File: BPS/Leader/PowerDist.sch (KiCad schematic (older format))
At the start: 15 parts, among them J5 PowerConn, U2 RI3-1205S, U3 NCP1117-3.3_SOT223

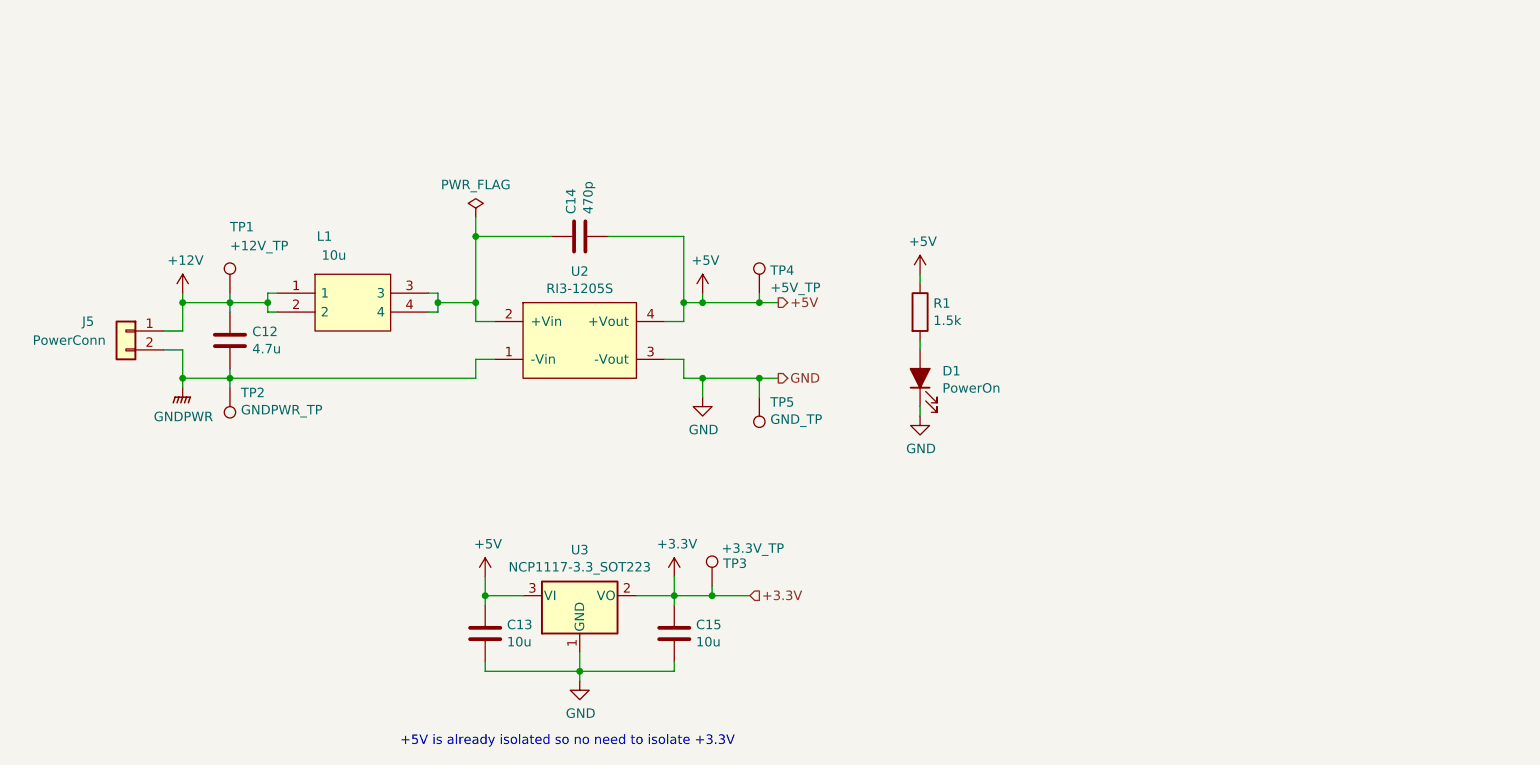
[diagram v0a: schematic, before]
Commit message: Places most components of leader board in their respective locations with nothing traced
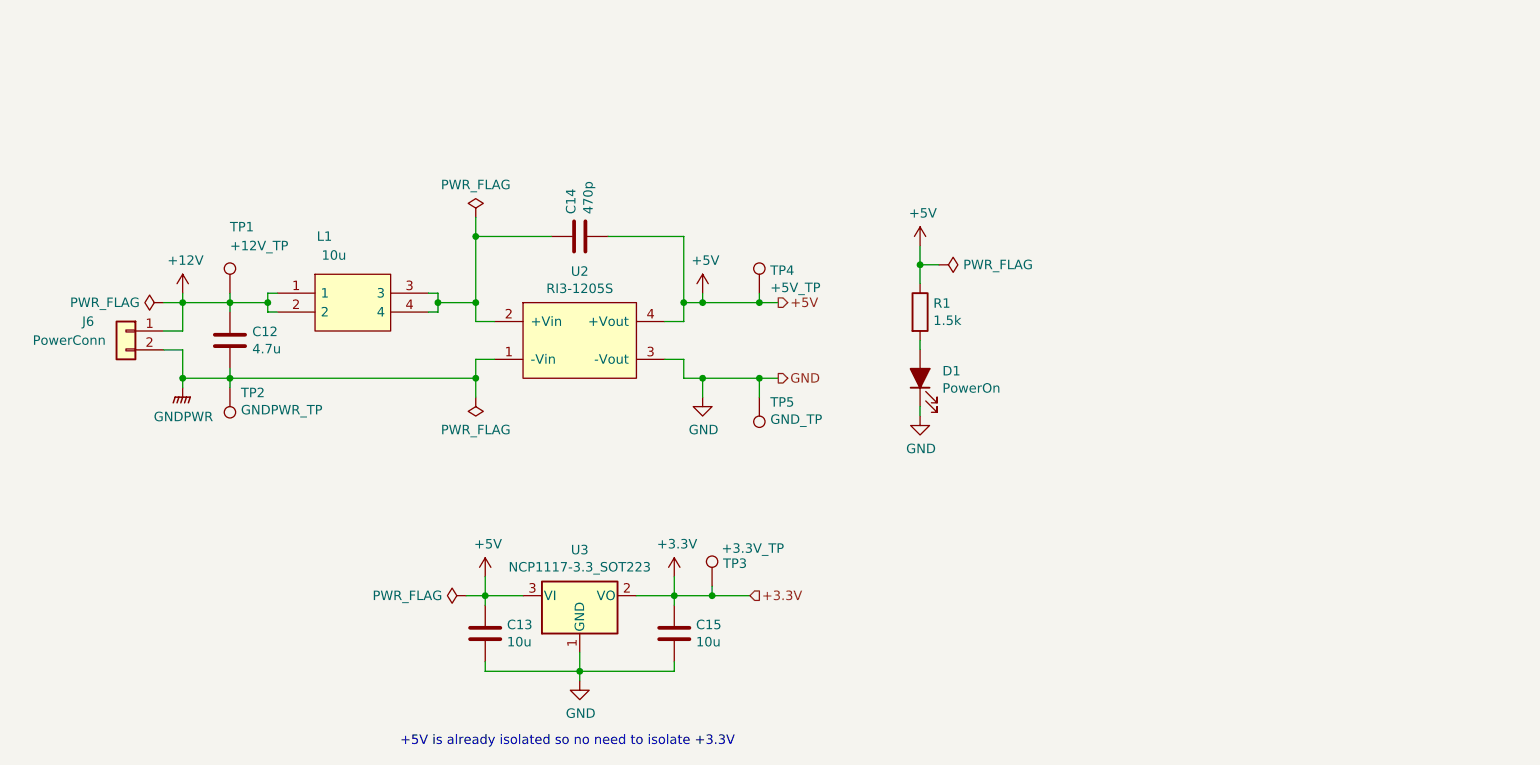
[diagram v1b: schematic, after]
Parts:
- J6: renamed from J5; footprint Connector_Molex:Molex_Micro-Fit_3.0_43650-0215_1x02_P3.00mm_Vertical -> UTSVT_Connectors:Molex_MicroFit3.0_1x2xP3.00mm_PolarizingPeg_Vertical
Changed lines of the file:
@@
 L power:+5V #PWR028
 U 1 1 5C58FEF6
-P 6350 3050
-F 0 "#PWR028" H 6350 2900 50  0001 C CNN
-F 1 "+5V" H 6365 3223 50  0000 C CNN
-F 2 "" H 6350 3050 50  0001 C CNN
-F 3 "" H 6350 3050 50  0001 C CNN
-	1    6350 3050
-	1    0    0    -1
-$EndComp
-Wire Wire Line
-	6350 3050 6350 3100
+P 6350 2900
+F 0 "#PWR028" H 6350 2750 50  0001 C CNN
+F 1 "+5V" H 6365 3073 50  0000 C CNN
+F 2 "" H 6350 2900 50  0001 C CNN
+F 3 "" H 6350 2900 50  0001 C CNN
+	1    6350 2900
+	1    0    0    -1
+$EndComp
+Wire Wire Line
+	6350 2900 6350 3000
 $Comp
 L power:GND #PWR027
@@
 	2900 3200 2900 3150
 $Comp
-L power:PWR_FLAG #FLG02
+L power:PWR_FLAG #FLG04
 U 1 1 5D8F68D6
 P 4000 2750
-F 0 "#FLG02" H 4000 2825 50  0001 C CNN
+F 0 "#FLG04" H 4000 2825 50  0001 C CNN
 F 1 "PWR_FLAG" H 4000 2923 50  0000 C CNN
 F 2 "" H 4000 2750 50  0001 C CNN
@@
 +5V is already isolated so no need to isolate +3.3V
 $Comp
-L Connector_Generic:Conn_01x02 J5
+L Connector_Generic:Conn_01x02 J6
 U 1 1 5F1149C6
 P 2150 3350
-F 0 "J5" H 2350 3400 50  0000 C CNN
+F 0 "J6" H 2350 3400 50  0000 C CNN
 F 1 "PowerConn" H 2450 3300 50  0000 C CNN
-F 2 "Connector_Molex:Molex_Micro-Fit_3.0_43650-0215_1x02_P3.00mm_Vertical" H 2150 3350 50  0001 C CNN
+F 2 "UTSVT_Connectors:Molex_MicroFit3.0_1x2xP3.00mm_PolarizingPeg_Vertical" H 2150 3350 50  0001 C CNN
 F 3 "~" H 2150 3350 50  0001 C CNN
 	1    2150 3350
@@
 Wire Wire Line
 	2450 3200 2450 3350
+$Comp
+L power:PWR_FLAG #FLG03
+U 1 1 5F1E78A7
+P 3950 4750
+F 0 "#FLG03" H 3950 4825 50  0001 C CNN
+F 1 "PWR_FLAG" V 3950 4877 50  0000 L CNN
+F 2 "" H 3950 4750 50  0001 C CNN
+F 3 "~" H 3950 4750 50  0001 C CNN
+	1    3950 4750
+	0    -1   -1   0
+$EndComp
+Wire Wire Line
+	3950 4750 4050 4750
+$Comp
+L power:PWR_FLAG #FLG05
+U 1 1 5F1EAFA2
+P 4000 3700
+F 0 "#FLG05" H 4000 3775 50  0001 C CNN
+F 1 "PWR_FLAG" H 4000 3873 50  0000 C CNN
+F 2 "" H 4000 3700 50  0001 C CNN
+F 3 "~" H 4000 3700 50  0001 C CNN
+	1    4000 3700
+	-1   0    0    1
+$EndComp
+Wire Wire Line
+	4000 3700 4000 3600
+Connection ~ 4000 3600
+$Comp
+L power:PWR_FLAG #FLG06
+U 1 1 5F1ED21F
+P 6450 3000
+F 0 "#FLG06" H 6450 3075 50  0001 C CNN
+F 1 "PWR_FLAG" V 6450 3128 50  0000 L CNN
+F 2 "" H 6450 3000 50  0001 C CNN
+F 3 "~" H 6450 3000 50  0001 C CNN
+	1    6450 3000
+	0    1    1    0
+$EndComp
+Wire Wire Line
+	6450 3000 6350 3000
+Connection ~ 6350 3000
+Wire Wire Line
+	6350 3000 6350 3100
+$Comp
+L power:PWR_FLAG #FLG02
+U 1 1 5F1F32D3
+P 2350 3200
+F 0 "#FLG02" H 2350 3275 50  0001 C CNN
+F 1 "PWR_FLAG" V 2350 3327 50  0000 L CNN
+F 2 "" H 2350 3200 50  0001 C CNN
+F 3 "~" H 2350 3200 50  0001 C CNN
+	1    2350 3200
+	0    -1   -1   0
+$EndComp
+Wire Wire Line
+	2350 3200 2450 3200
 $EndSCHEMATC

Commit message: Finished leader board
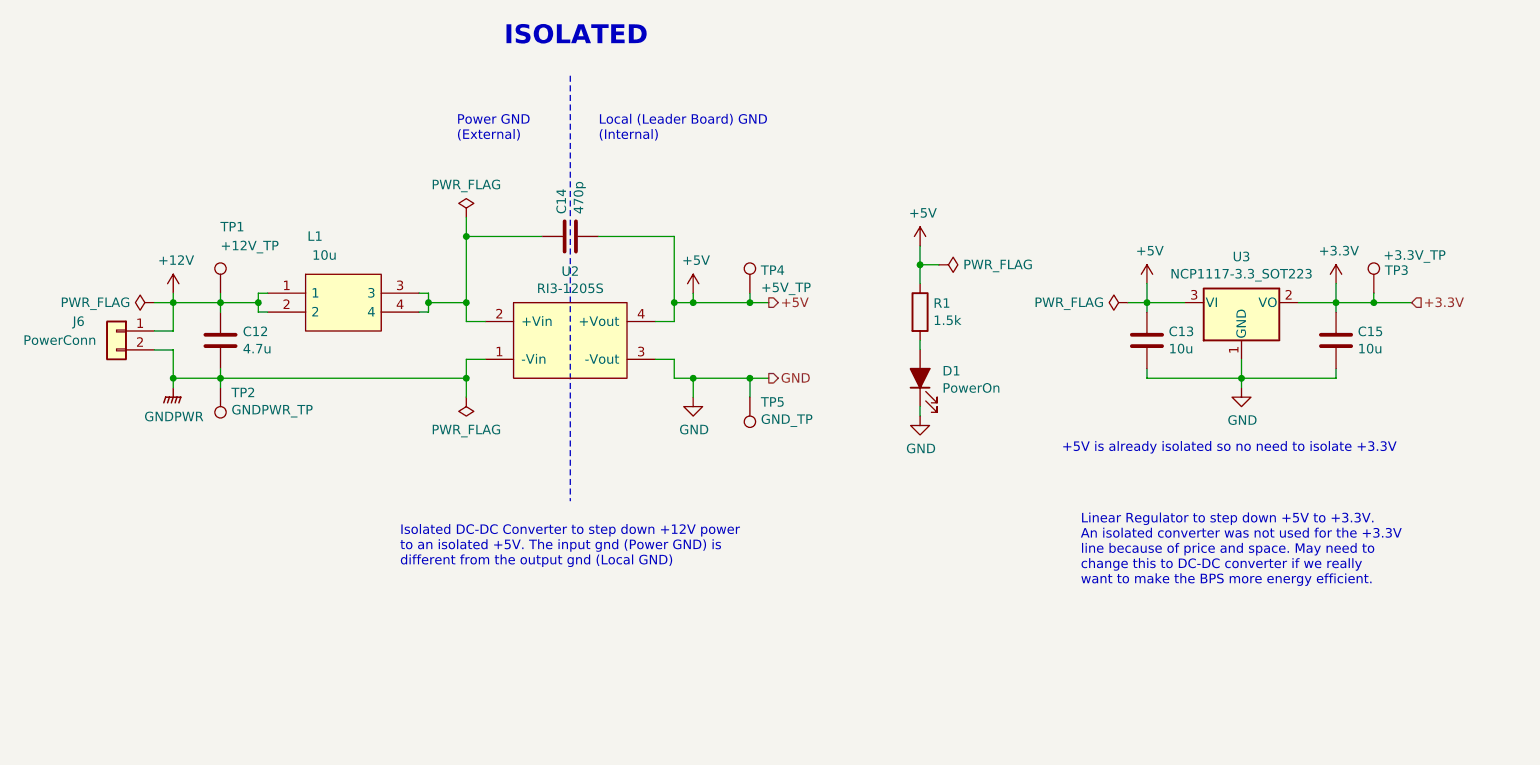
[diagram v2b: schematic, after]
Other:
- note added: "ISOLATED"
- note added: "Isolated DC-DC Converter to step down +12V power\nto an isolated +5V. The input gnd (Power GND) is\ndifferent from the output gnd (Local GND)"
- note added: "Linear Regulator to step down +5V to +3.3V.\nAn isolated converter was not used for the +3.3V\nline because of price and space. May need to\nchange this to DC-DC converter if we really\nwant to make the BPS more energy efficient."
- note added: "Local (Leader Board) GND\n(Internal)"
- note added: "Power GND\n(External)"
- moved on the sheet: C12, C13, C14, C15, J6, L1, TP1, TP2, TP3, TP4, TP5, U2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

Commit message: Simplifies dc-dc converter schematics
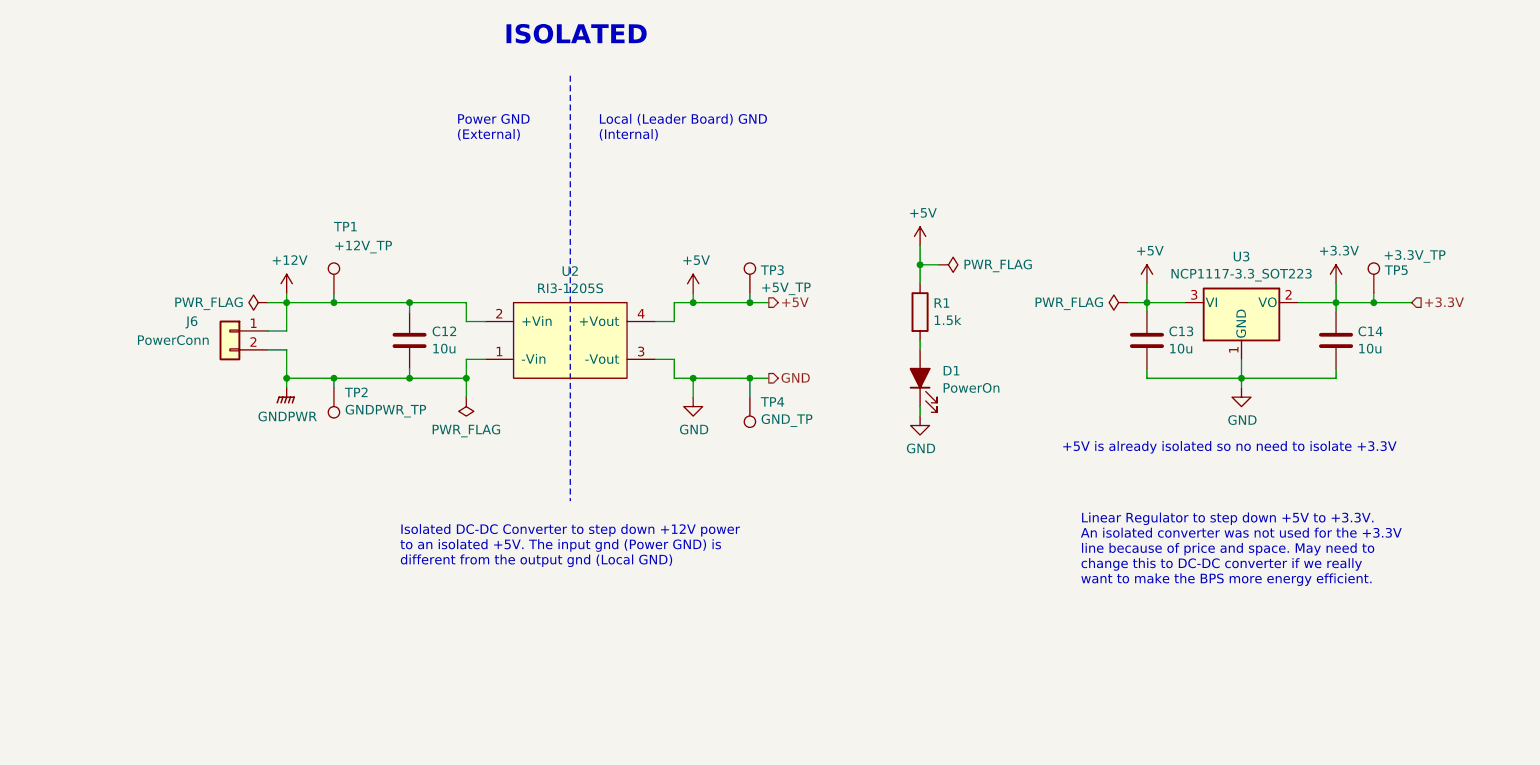
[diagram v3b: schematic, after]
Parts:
- removed C14: 470p, Capacitor_SMD:C_2220_5650Metric, symbol Device:C
- removed L1: 10u, UTSVT_BPS:SRF0905A, symbol utsvt-bps:SRF0905-100Y
- C12: value 4.7u -> 10u; footprint Capacitor_SMD:C_0805_2012Metric -> UTSVT_Passive:C_2220_5750Metric
- renumbered C15 to C14, TP4 to TP3, TP5 to TP4, TP3 to TP5
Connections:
- net +12V: now also U2.2 (+Vin)
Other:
- moved on the sheet: C12, J6, TP1, TP2
